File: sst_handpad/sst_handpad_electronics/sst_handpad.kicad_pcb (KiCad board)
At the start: 2 copper layers, 61 x 102.6 mm, 26 parts, among them J1 GPS, Q1 2N7002PW, Q2 2N7002PW, U1 AdafruitItsyM0, U2 MC14504B

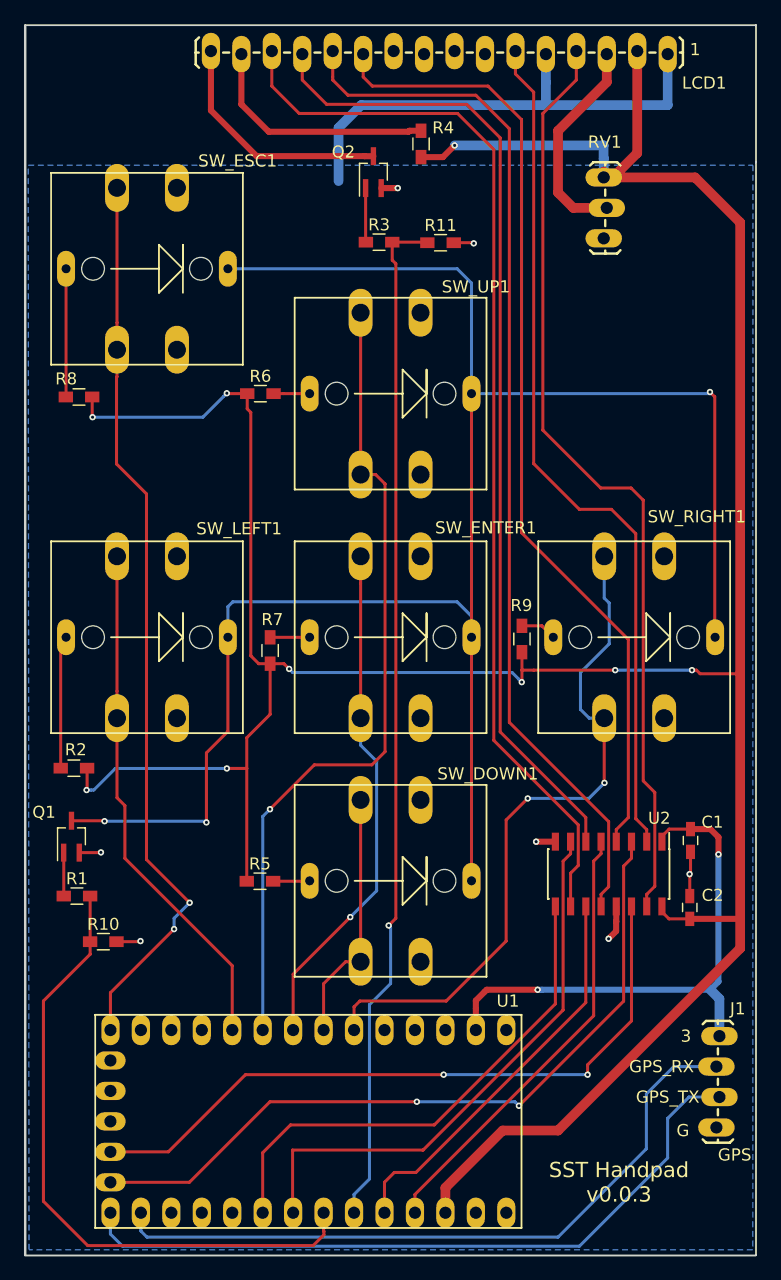
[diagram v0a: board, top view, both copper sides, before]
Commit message: Updated handpad with bosses and virtical micro, and rotated lcd pins
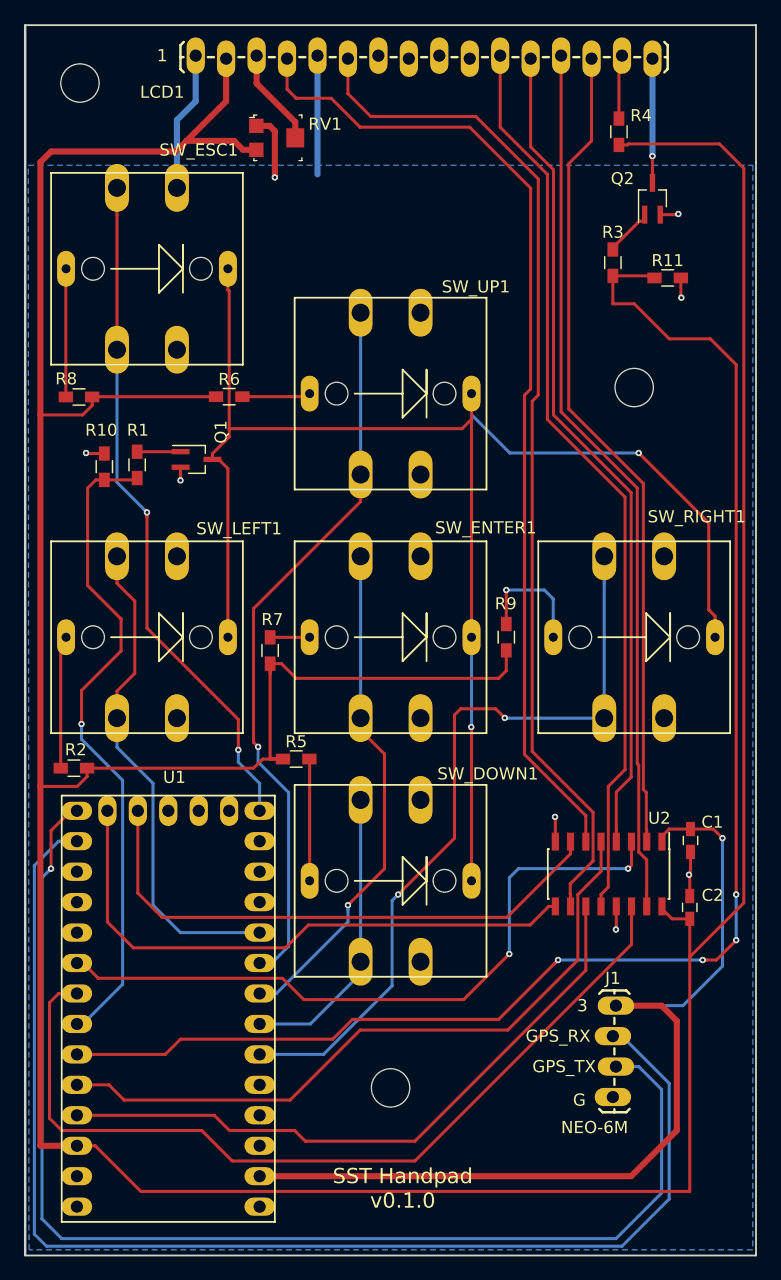
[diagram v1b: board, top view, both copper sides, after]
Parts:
- added H1: MountingHole, Mounting_Holes:MountingHole_3.2mm_M3, F.Cu at (137.2, 126.7)
- added H2: MountingHole, Mounting_Holes:MountingHole_3.2mm_M3, F.Cu at (157.5, 68.3)
- added H3: MountingHole, Mounting_Holes:MountingHole_3.2mm_M3, F.Cu at (111.3, 42.9)
- J1: value GPS -> NEO-6M
- R2, R5, R6, R7, R8, R9: value 330 -> 1k
- RV1: value 10k -> TC33X-2-103E; footprint Connectors:1X03_LOCK_LONGPADS -> digikey-footprints:Trimpot_3.8mmx3.6mm_TC33X-2-103E
- moved R10 39.6 mm to (113.3, 74.9), turned to 90 degrees
- moved LCD1 39.4 mm to (120.9, 40.8), turned to 0 degrees
- moved R1 36.3 mm to (116.0, 74.8), turned to 270 degrees
- moved Q1 33.2 mm to (121.0, 74.3), turned to 0 degrees
- moved RV1 28.4 mm to (127.8, 47.5), turned to 270 degrees
- moved Q2 23.4 mm to (159.0, 52.6)
- moved R3 19.6 mm to (155.7, 57.9), turned to 270 degrees
- moved R11 19.2 mm to (160.3, 59.2)
- moved R4 16.5 mm to (156.2, 47.0)
- moved U1 15.0 mm to (118.6, 120.1), turned to 90 degrees
- moved R5 10.6 mm to (129.3, 99.3)
- moved J1 9.00 mm to (155.7, 127.5)
- moved R6 2.62 mm to (123.7, 69.1)
- moved R9 1.31 mm to (146.8, 89.2)
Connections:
- U2 pad 10: DB7LCD -> ENLCD
- U2 pad 11: DB5MC -> DB4MC
- U2 pad 12: DB5LCD -> DB4LCD
- U2 pad 14: RSMC -> DB6MC
- U2 pad 15: RSLCD -> DB6LCD
- U2 pad 2: ENLCD -> DB7LCD
- U2 pad 3: ENMC -> DB7MC
- U2 pad 4: DB4LCD -> DB5LCD
- U2 pad 5: DB4MC -> DB5MC
- U2 pad 6: DB6LCD -> RSLCD
- U2 pad 7: DB6MC -> RSMC
- U2 pad 9: DB7MC -> ENMC
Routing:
- net +5V: track 263.3 -> 339.0 mm, vias 9 -> 0
- net TXMC: track 58.3 -> 106.6 mm
- net RXMC: track 60.1 -> 102.7 mm, vias 0 -> 1
- net PWM_LCD: track 85.6 -> 125.2 mm, vias 1 -> 4
- net B_LEDS: track 164.0 -> 130.6 mm, vias 3 -> 2
- net +3V3: track 45.3 -> 78.1 mm, vias 2 -> 1
- net DB6MC: track 47.0 -> 72.9 mm
- net DB5MC: track 33.6 -> 57.8 mm
- net DB7LCD: track 89.9 -> 68.8 mm
- net B_ESC: track 75.5 -> 56.9 mm
- net DB5LCD: track 87.4 -> 69.3 mm
- net DB4MC: track 37.4 -> 54.6 mm
- net GND: track 56.4 -> 40.8 mm, vias 7 -> 8
- net DB7MC: track 42.7 -> 57.8 mm, vias 0 -> 2
- net Net-(LCD1-Pad15): track 20.2 -> 5.36 mm
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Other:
- outline, holes or cut-outs redrawn
- board text added: "SST Handpad v0.1.0"
- board text removed: "SST Handpad v0.0.3"

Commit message: Added models and missing files
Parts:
- SW_DOWN1, SW_ENTER1, SW_ESC1, SW_LEFT1, SW_RIGHT1, SW_UP1: value SW_Push_LED -> ILS_TA_BUTTON; footprint custom_footprints:MPJA_LED_SWITCH -> custom_footprints:ILS_TA_BUTTON
- turned SW_DOWN1 to 270 degrees
- turned SW_ENTER1 to 270 degrees
- turned SW_ESC1 to 270 degrees
- turned SW_LEFT1 to 270 degrees
- turned SW_RIGHT1 to 270 degrees
- turned SW_UP1 to 270 degrees
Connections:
- R2 pad 1: +5V -> Net-(R2-Pad1)
- R2 pad 2: Net-(R2-Pad2) -> +5V
- SW_DOWN1 pad 2: GND -> (no net)
- SW_DOWN1 pad 3: B_LEDS -> (no net)
- SW_DOWN1 pad 4: Net-(R5-Pad2) -> GND
- SW_ENTER1 pad 2: GND -> (no net)
- SW_ENTER1 pad 3: B_LEDS -> (no net)
- SW_ENTER1 pad 4: Net-(R7-Pad2) -> GND
- SW_ESC1 pad 2: GND -> (no net)
- SW_ESC1 pad 3: B_LEDS -> (no net)
- SW_ESC1 pad 4: Net-(R8-Pad2) -> GND
- SW_LEFT1 pad 2: GND -> (no net)
- SW_LEFT1 pad 3: B_LEDS -> (no net)
- SW_LEFT1 pad 4: Net-(R2-Pad2) -> GND
- SW_RIGHT1 pad 2: GND -> (no net)
- SW_RIGHT1 pad 3: B_LEDS -> (no net)
- SW_RIGHT1 pad 4: Net-(R9-Pad2) -> GND
- SW_UP1 pad 2: GND -> (no net)
- SW_UP1 pad 3: B_LEDS -> (no net)
- SW_UP1 pad 4: Net-(R6-Pad2) -> GND
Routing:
- net B_LEDS: track 130.6 -> 147.1 mm, vias 2 -> 1
- net Net-(R2-Pad1): track 0.00 -> 12.7 mm
- net Net-(R2-Pad2): track 11.1 -> 0.00 mm
- net +5V: track 339.0 -> 345.1 mm, vias 0 -> 2
- net B_RIGHT: track 64.7 -> 59.6 mm, vias 2 -> 3
- net DB7LCD: track 68.8 -> 73.8 mm
- net DB6LCD: track 73.9 -> 78.8 mm
- net B_LEFT: track 41.4 -> 36.6 mm
- net Net-(R7-Pad2): track 3.30 -> 7.15 mm
- net Net-(R6-Pad2): track 5.72 -> 9.57 mm
- net Net-(R5-Pad2): track 10.2 -> 14.0 mm
- net B_DOWN: track 24.7 -> 21.5 mm
- net Net-(R8-Pad2): track 10.7 -> 13.5 mm
- net PWM_BUTTONS: track 55.0 -> 52.3 mm
- net Net-(R9-Pad2): track 10.3 -> 12.7 mm
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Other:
- board text added: "SST Handpad v0.2.0"
- board text removed: "SST Handpad v0.1.0"
